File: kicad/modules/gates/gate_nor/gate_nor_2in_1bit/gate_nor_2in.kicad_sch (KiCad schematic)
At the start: 4 parts, among them Q201 NMOS, Q202 PMOS, Q203 PMOS, Q204 NMOS

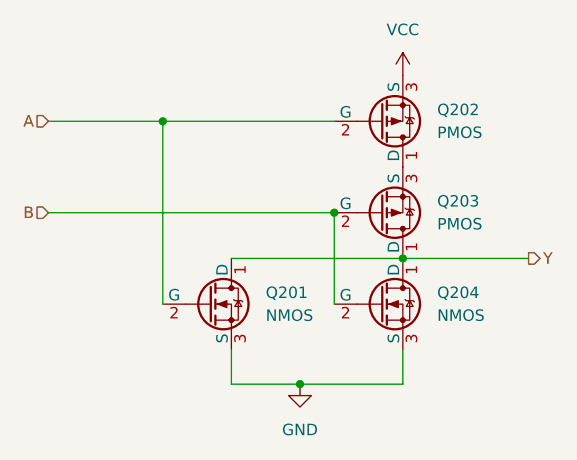
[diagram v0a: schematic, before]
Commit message: feat: complete circuit designs for all ALU components
* Designed all gate modules: AND, OR, NOT, NAND, NOR, XOR (1-bit and 8-bit variants)

* Completed multiplexer hierarchy: 2:1, 4:1, and 8:1 8-bit muxes

* Finalized add_sub board schematic and LED panel designs

* Added new board modules: flags, main_control, main_logic

* Updated Logisim top-level ALU circuit

* Note: KiCad directory path errors to be resolved next (iCloud sync issue), then begin PCB routing
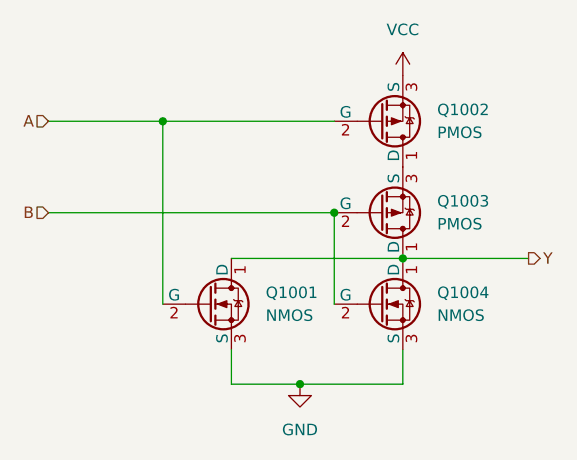
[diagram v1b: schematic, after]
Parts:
- renumbered Q201 to Q1001, Q202 to Q1002, Q203 to Q1003, Q204 to Q1004

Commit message: Fix KiCad file paths and complete core circuit design
- Fixed file path errors across all KiCad schematics and projects
- Completed core circuit designs:
  * Adder and subtractor modules (adder2, adder8)
  * LED panels (led_panel_1) with display circuits
  * Flag LED circuits for status indicators
  * All dependent logic gate modules (AND, OR, NOT, NAND, NOR, XOR)
  * All multiplexer modules (2:1, 4:1, 8:1, 8-bit)
  * Main control board schematics
  * Flags board schematics
- Updated .gitignore to exclude KiCad backups, cache files, and lock files
- Ready for pin placement and routing of control buses, power rails, and inter-board signals
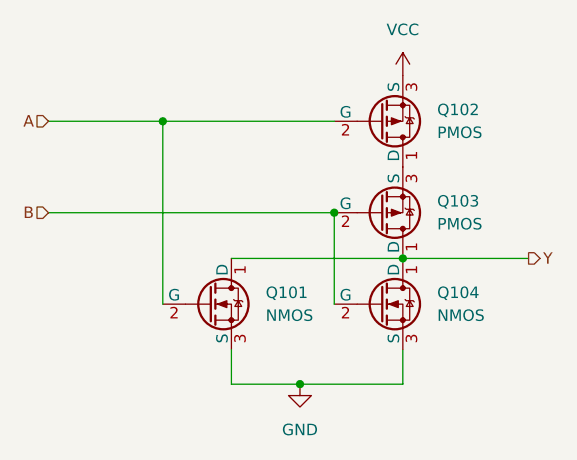
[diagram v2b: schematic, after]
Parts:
- renumbered Q1001 to Q101, Q1002 to Q102, Q1003 to Q103, Q1004 to Q104
